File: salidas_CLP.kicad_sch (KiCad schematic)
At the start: 42 parts

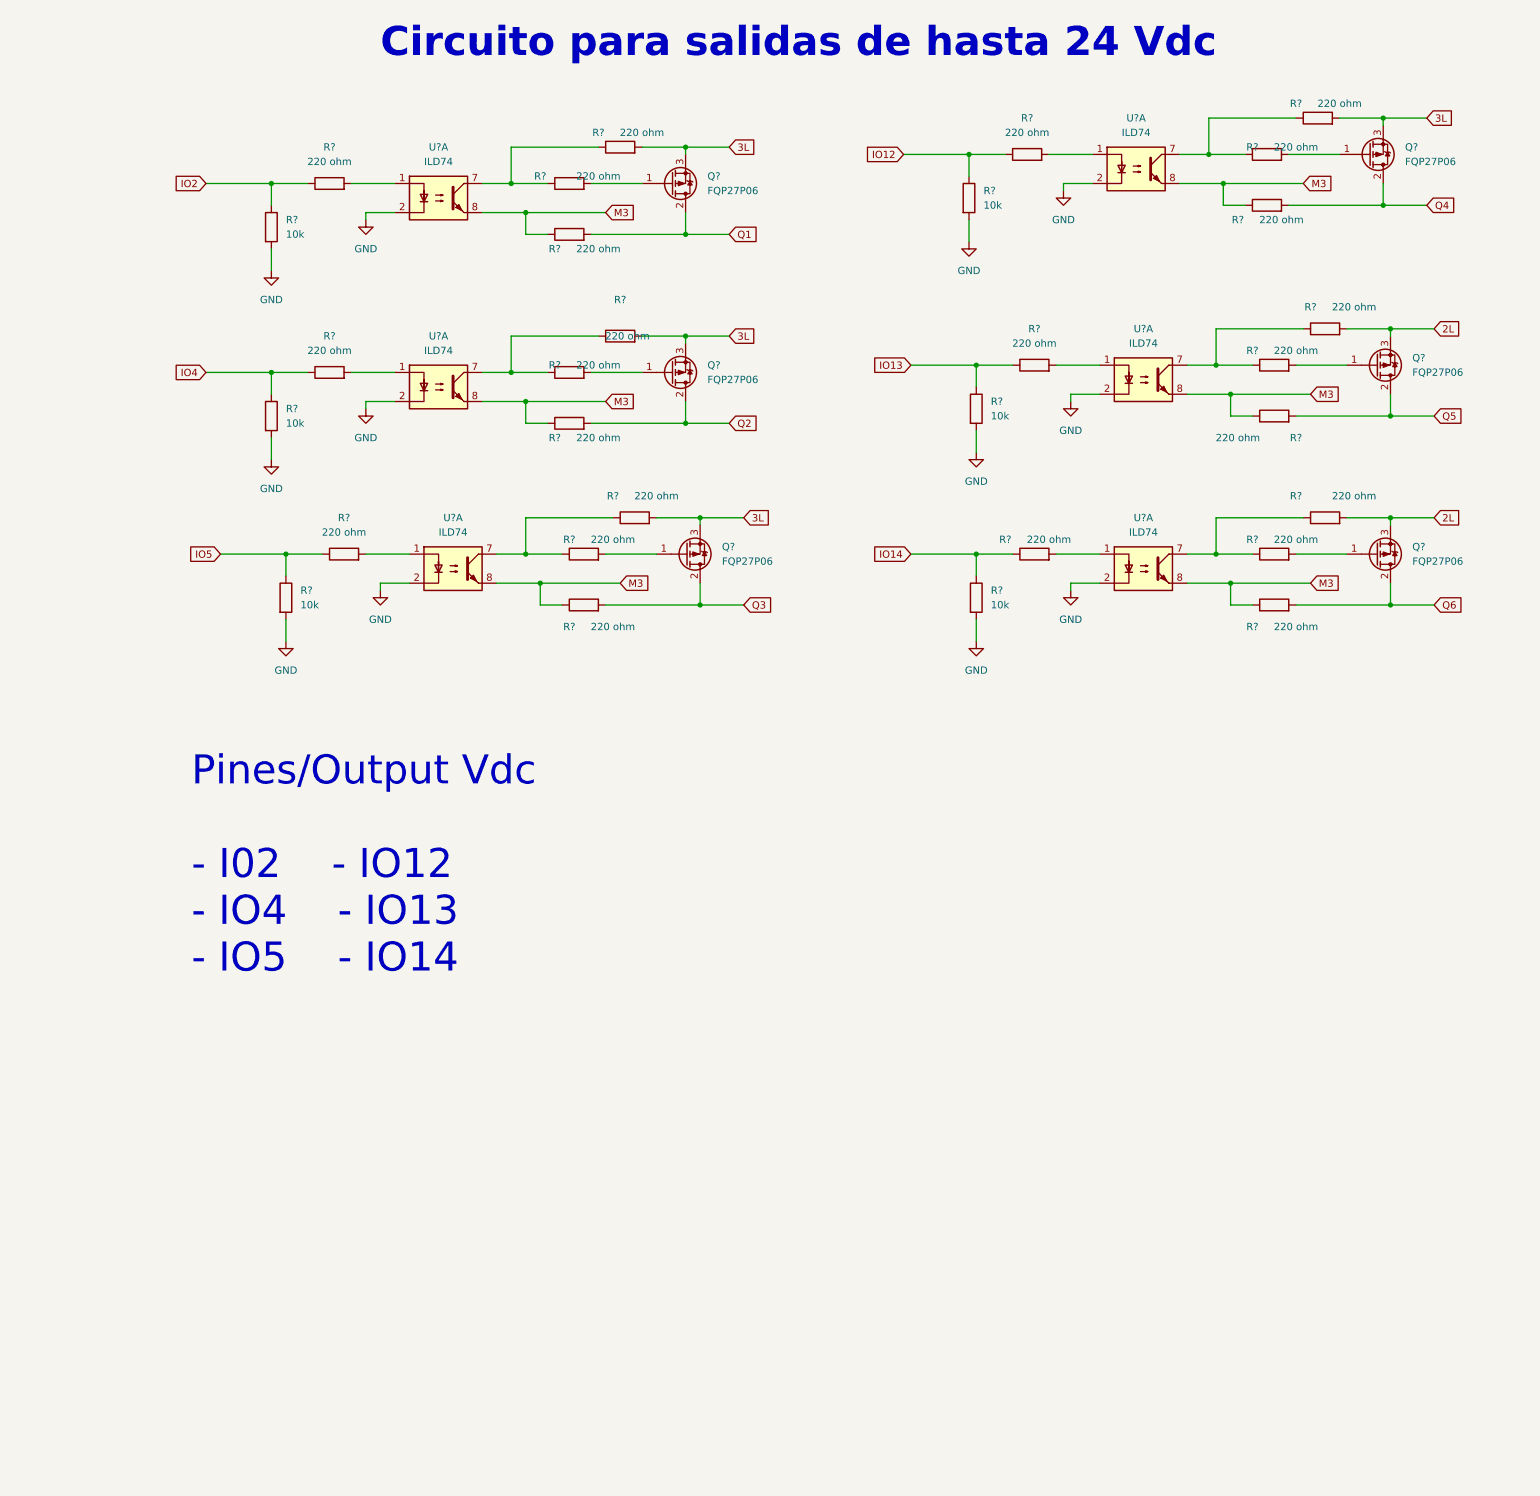
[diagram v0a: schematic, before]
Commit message: Esquema con comentarios
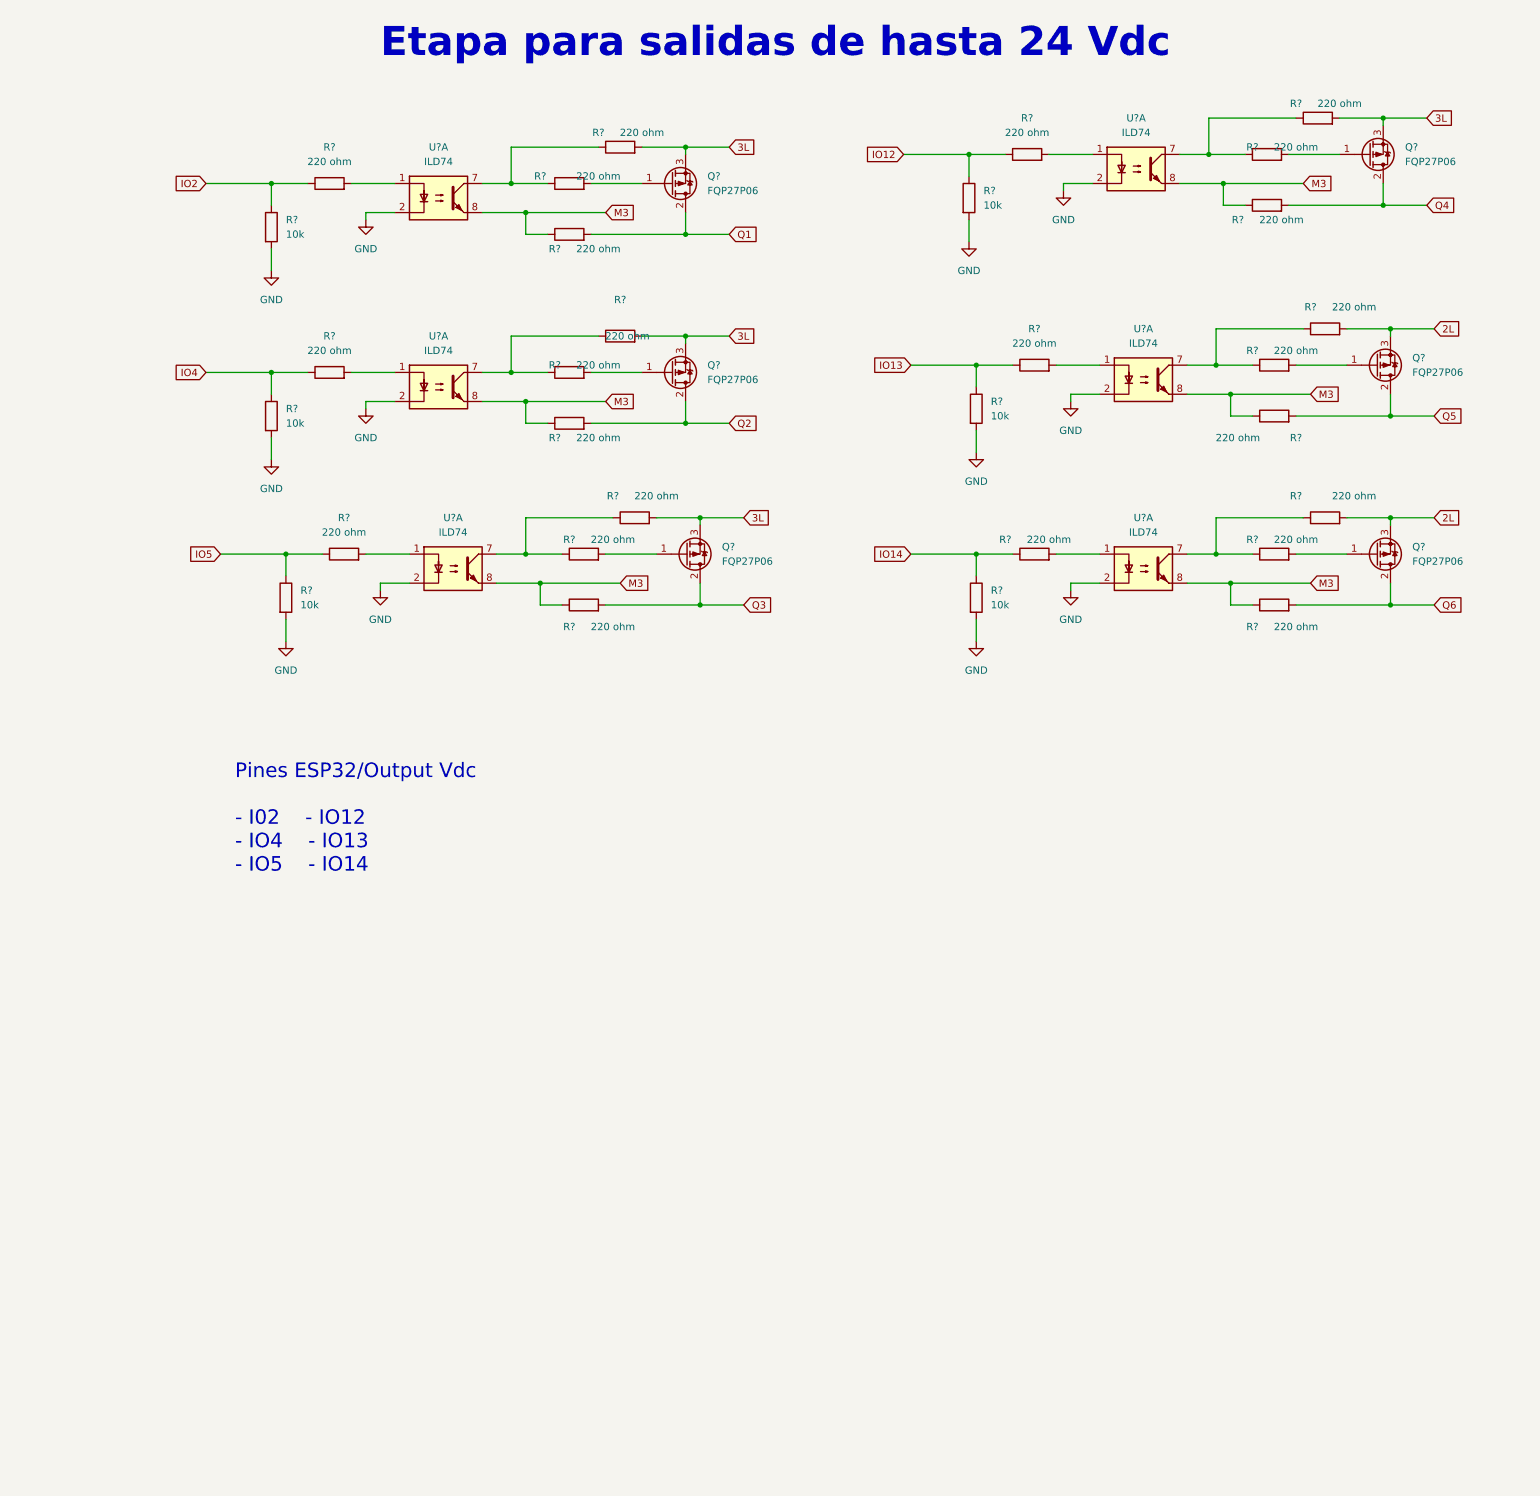
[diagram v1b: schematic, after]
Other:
- note added: "Etapa para salidas de hasta 24 Vdc"
- note added: "Pines ESP32/Output Vdc - I02 - IO12 - IO4 - IO13 - IO5 - IO14"
- note removed: "Circuito para salidas de hasta 24 Vdc"
- note removed: "Pines/Output Vdc - I02 - IO12 - IO4 - IO13 - IO5 - IO14"
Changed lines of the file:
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@@
     (stroke (width 0) (type default) (color 0 0 0 0))
   )
-  (text "Circuito para salidas de hasta 24 Vdc" (at 76.2 30.48 0)
+  (text "Etapa para salidas de hasta 24 Vdc" (at 76.2 30.48 0)
     (effects (font (size 5.08 5.08) (thickness 1.016) bold) (justify left bottom))
   )
-  (text "Pines/Output Vdc\n\n- I02	- IO12\n- IO4	- IO13\n- IO5	- IO14"
-    (at 43.18 190.5 0)
-    (effects (font (size 5.08 5.08)) (justify left bottom))
+  (text "Pines ESP32/Output Vdc\n\n- I02	- IO12\n- IO4	- IO13\n- IO5	- IO14"
+    (at 50.8 172.72 0)
+    (effects (font (size 2.54 2.54)) (justify left bottom))
   )
   (global_label "Q5" (shape input) (at 260.35 92.71 0) (fields_autoplaced)

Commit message: update esq raiz
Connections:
- net IO2 renamed IO02
- net IO4 renamed IO04
- net IO5 renamed IO05
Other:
- note added: "Etapa: Salidas 24 Vdc"
- note removed: "Etapa para salidas de hasta 24 Vdc"
- moved on the sheet: Q?, R?, U?A

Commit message: update esq raiz salidas
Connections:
- net 2L: now also Q?.3 (S), R?.2
- net 3L: no longer Q?.3 (S), R?.2
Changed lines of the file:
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@@
     (effects (font (size 1.27 1.27)) (justify right))
   )
-  (hierarchical_label "3L" (shape input) (at 259.08 46.99 0)
+  (hierarchical_label "2L" (shape input) (at 259.08 46.99 0)
     (effects (font (size 1.27 1.27)) (justify left))
   )

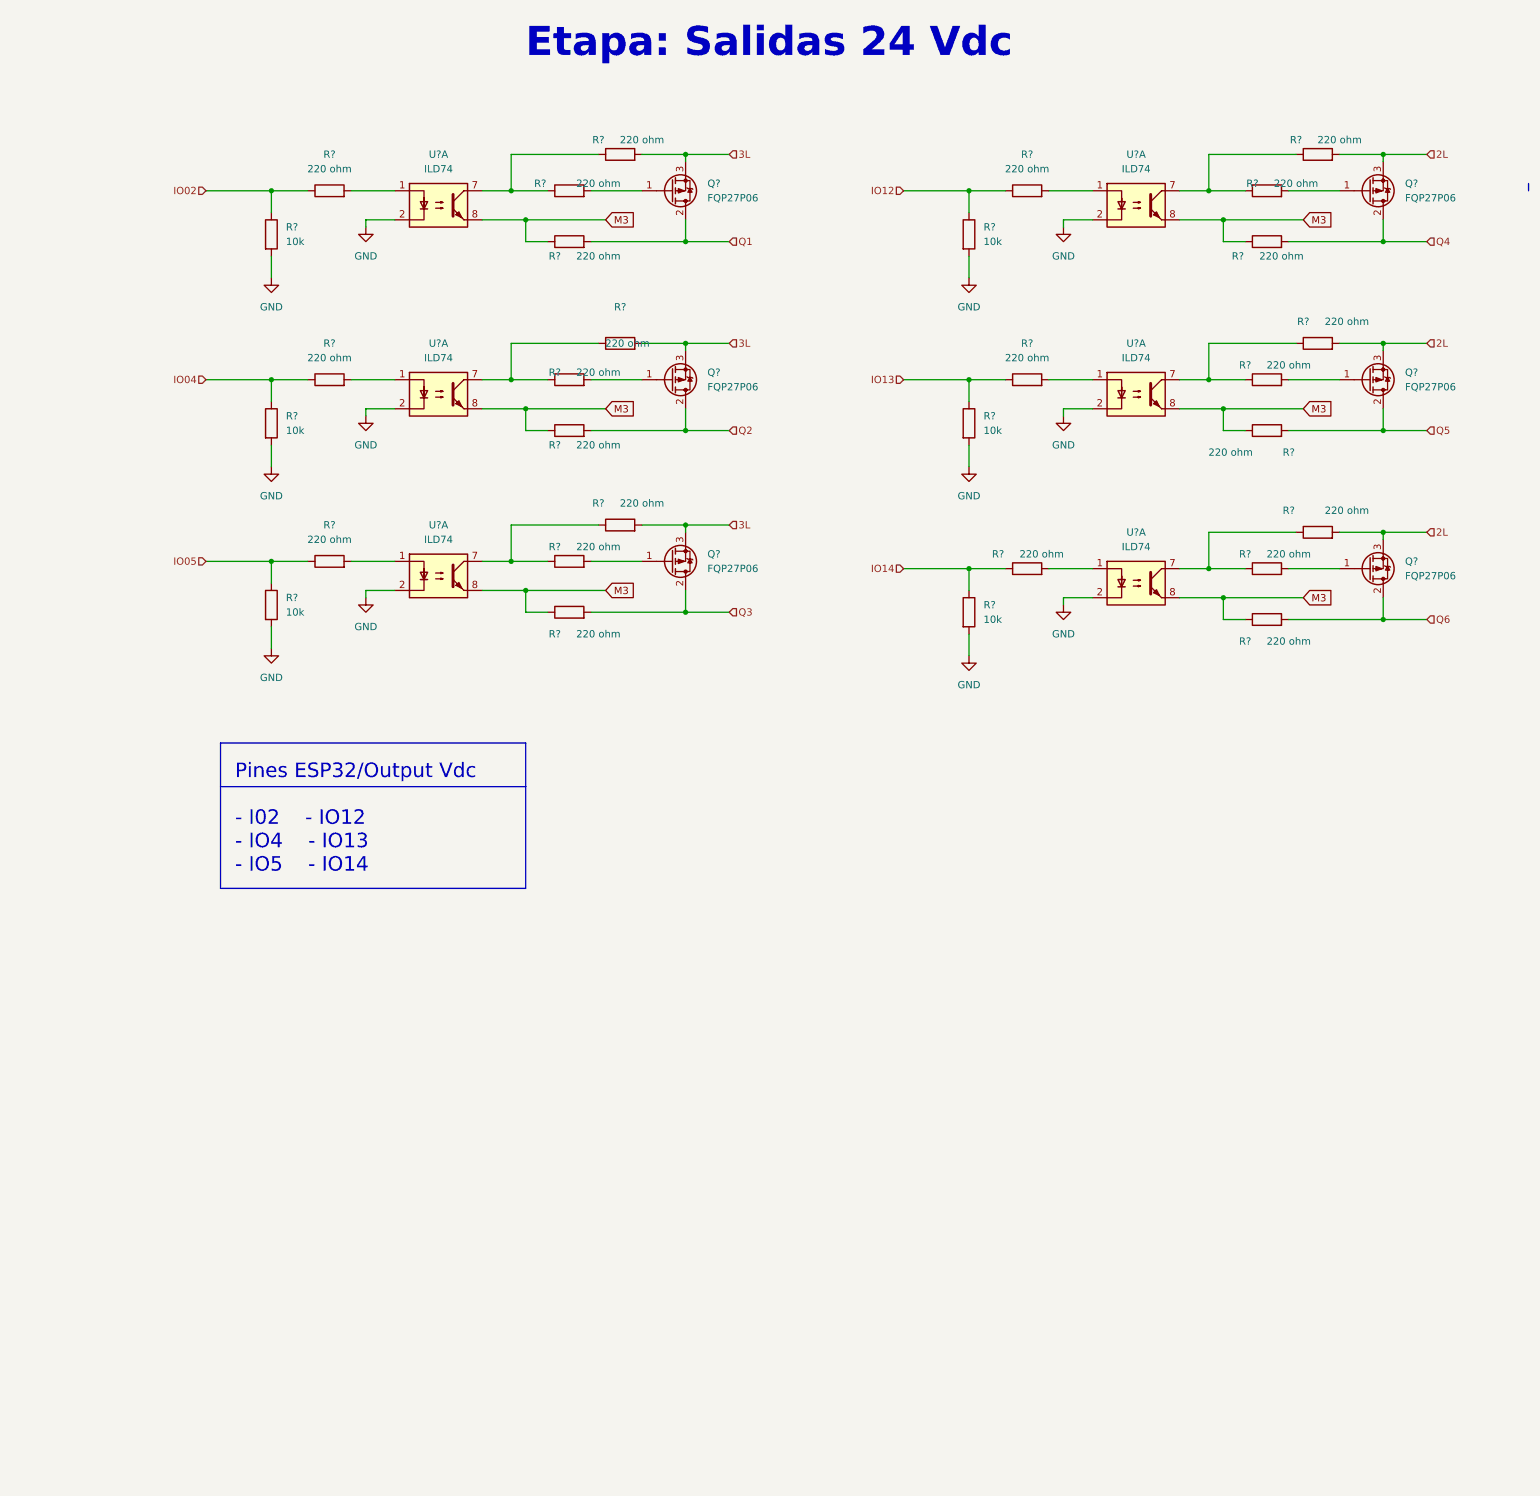
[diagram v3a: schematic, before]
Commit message: add salidas separadas 1,2,3
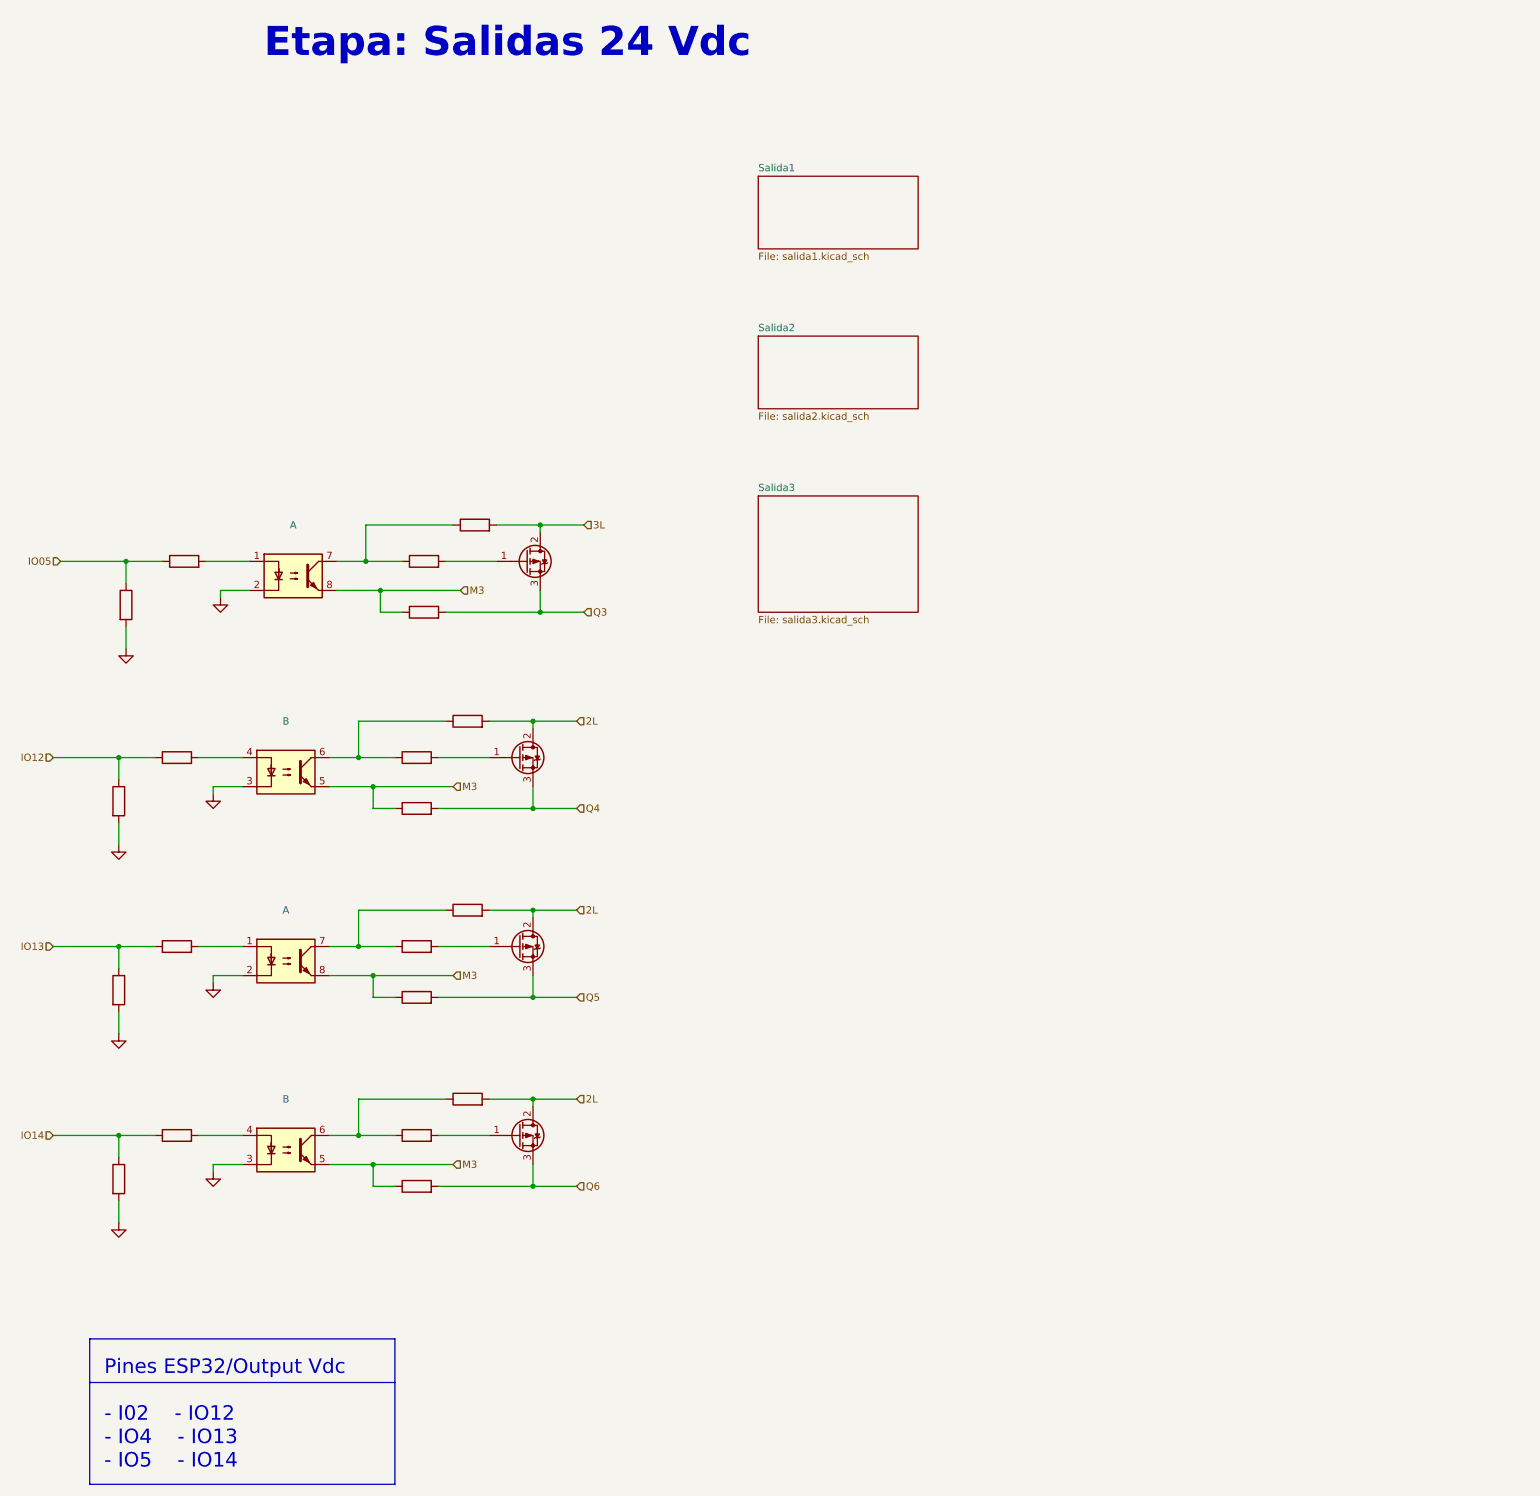
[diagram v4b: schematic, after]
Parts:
- removed Q? (x6): FQP27P06, Package_TO_SOT_SMD:TO-252-2_TabPin1, symbol Transistor_FET:FQP27P06
- removed R? (x2): 10k, Resistor_SMD:R_0603_1608Metric_Pad0.98x0.95mm_HandSolder, symbol Device:R
- removed R? (x8): 220 ohm, Resistor_SMD:R_0603_1608Metric_Pad0.98x0.95mm_HandSolder, symbol Device:R
- removed U? (x6): ILD74, Package_DIP:DIP-4_W7.62mm, symbol Isolator:ILD74
- added ? (x4): (no value), symbol Isolator:ILD74
- added ? (x4): (no value), symbol Transistor_FET:FQP27P06
- ? (x4): renamed from R?; value 10k -> (none); footprint Resistor_SMD:R_0603_1608Metric_Pad0.98x0.95mm_HandSolder -> (none)
- ? (x15): renamed from R?; value 220 ohm -> (none); footprint Resistor_SMD:R_0603_1608Metric_Pad0.98x0.95mm_HandSolder -> (none)
- ?: renamed from R?; value 220 ohm -> (none); footprint Resistor_SMD:R_0612_1632Metric -> (none)
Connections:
- net 2L: now also ?.2 (D), ?.2 (D), ?.2 (D)
- net 3L: now also ?.2 (D)
- net GND: now also ?.2, ?.2, ?.3, ?.3
- net M3: now also ?.5, ?.5, ?.8, ?.8
- net Q3: now also ?.3 (S)
- net Q4: now also ?.3 (S)
- net Q5: now also ?.3 (S)
- net Q6: now also ?.3 (S)
- net at ?.2: now also ?.4 (x2)
- net at ?.1, ?.1: now also ?.7 (x2)
- net at ?.2: now also ?.1 (G) (x4)
- net at ?.2: now also ?.1 (x2)
- net at ?.1, ?.1: now also ?.6 (x2)
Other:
- added sheet Salida1 (salida1.kicad_sch)
- added sheet Salida2 (salida2.kicad_sch)
- added sheet Salida3 (salida3.kicad_sch)
- company: (none) -> INTEAMBI
